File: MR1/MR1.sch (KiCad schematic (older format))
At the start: 16 parts, among them J1 Conn_01x04_Male, J2 Conn_01x04_Male, J3 Conn_01x04_Male, J4 Conn_01x04_Male, J5 Conn_01x02_Male, J6 Conn_01x04_Male, J7 Conn_01x04_Male, J8 Conn_01x04_Male, Q1 2SC1815, U5 LPC1768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

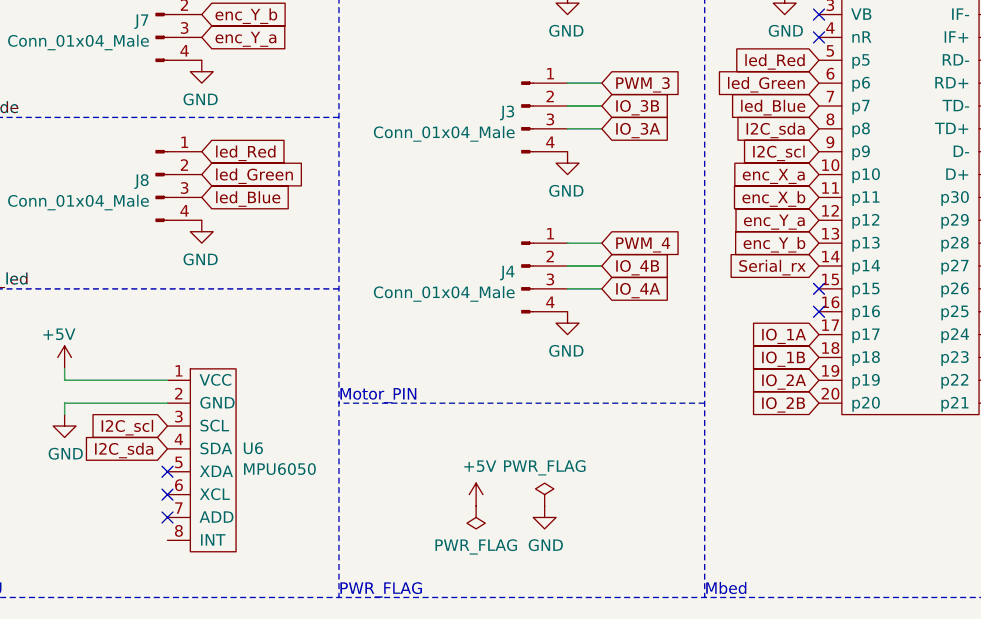
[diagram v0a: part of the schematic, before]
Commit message: update:MR1の基板完成
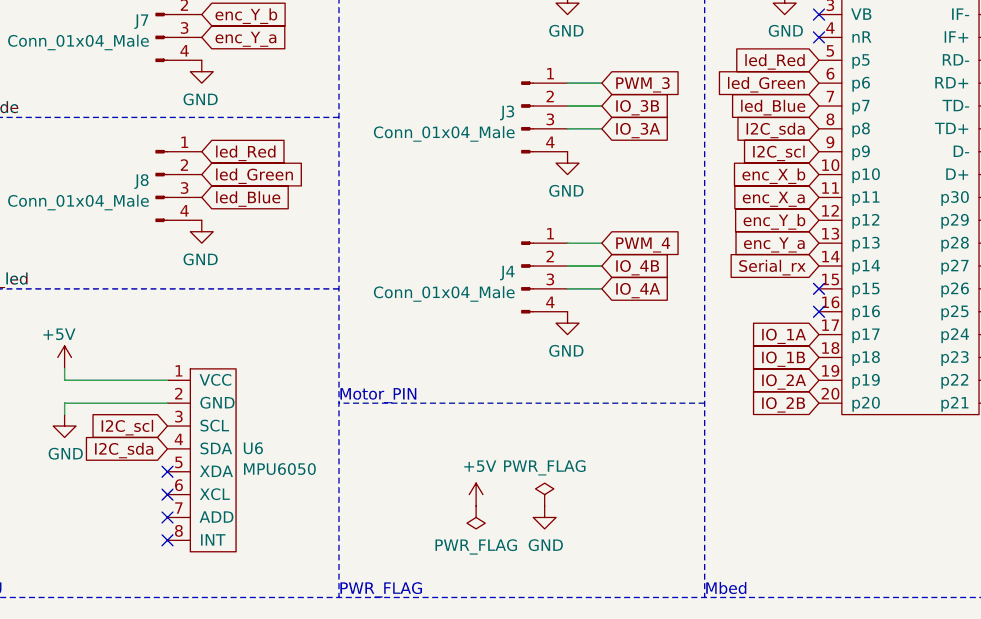
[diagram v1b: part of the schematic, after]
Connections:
- net enc_X_a: now also U5.11 (p11); no longer U5.10 (p10)
- net enc_X_b: now also U5.10 (p10); no longer U5.11 (p11)
- net enc_Y_a: now also U5.13 (p13); no longer U5.12 (p12)
- net enc_Y_b: now also U5.12 (p12); no longer U5.13 (p13)
- no-connect marks 18 -> 19
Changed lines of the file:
@@
 EESchema Schematic File Version 4
+LIBS:MR1-cache
 EELAYER 29 0
 EELAYER END
@@
 Text Notes 3200 4950 0    50   ~ 0
 Motor_PIN
-Text GLabel 5300 4150 0    50   Input ~ 0
+Text GLabel 5300 4250 0    50   Input ~ 0
 enc_Y_a
+Text GLabel 5300 4050 0    50   Input ~ 0
+enc_X_a
 Text GLabel 5300 3950 0    50   Input ~ 0
-enc_X_a
-Text GLabel 5300 4050 0    50   Input ~ 0
 enc_X_b
 Text GLabel 2600 3250 2    50   Input ~ 0
@@
 	1    0    0    -1
 $EndComp
-Text GLabel 5300 4250 0    50   Input ~ 0
+Text GLabel 5300 4150 0    50   Input ~ 0
 enc_Y_b
 Wire Notes Line
@@
 Text Label 1550 4450 0    50   ~ 0
 tape_led
+NoConn ~ 2450 5550
 $EndSCHEMATC

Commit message: fix: MR1
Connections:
- net I2C_scl: now also U5.10 (p10); no longer U5.9 (p9)
- net I2C_sda: now also U5.9 (p9); no longer U5.8 (p8)
- net enc_X_a: now also U5.12 (p12); no longer U5.11 (p11)
- net enc_X_b: now also U5.11 (p11); no longer U5.10 (p10)
- net enc_Y_a: now also U5.16 (p16); no longer U5.13 (p13)
- net enc_Y_b: now also U5.15 (p15); no longer U5.12 (p12)
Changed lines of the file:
@@
 Text GLabel 5300 4350 0    50   Input ~ 0
 Serial_rx
+Text GLabel 5300 3950 0    50   Input ~ 0
+I2C_scl
 Text GLabel 5300 3850 0    50   Input ~ 0
-I2C_scl
-Text GLabel 5300 3750 0    50   Input ~ 0
 I2C_sda
 Text GLabel 5300 4650 0    50   Input ~ 0
@@
 NoConn ~ 6100 3850
 NoConn ~ 6100 3950
-NoConn ~ 5300 4450
-NoConn ~ 5300 4550
 NoConn ~ 5300 3250
 NoConn ~ 5300 3350
@@
 Text Notes 3200 4950 0    50   ~ 0
 Motor_PIN
-Text GLabel 5300 4250 0    50   Input ~ 0
+Text GLabel 5300 4550 0    50   Input ~ 0
 enc_Y_a
-Text GLabel 5300 4050 0    50   Input ~ 0
-enc_X_a
-Text GLabel 5300 3950 0    50   Input ~ 0
-enc_X_b
 Text GLabel 2600 3250 2    50   Input ~ 0
 enc_Y_b
@@
 	1    0    0    -1
 $EndComp
-Text GLabel 5300 4150 0    50   Input ~ 0
+Text GLabel 5300 4450 0    50   Input ~ 0
 enc_Y_b
 Wire Notes Line
@@
 tape_led
 NoConn ~ 2450 5550
+NoConn ~ 5300 4250
+Text GLabel 5300 4050 0    50   Input ~ 0
+enc_X_b
+Text GLabel 5300 4150 0    50   Input ~ 0
+enc_X_a
+NoConn ~ 5300 3750
 $EndSCHEMATC

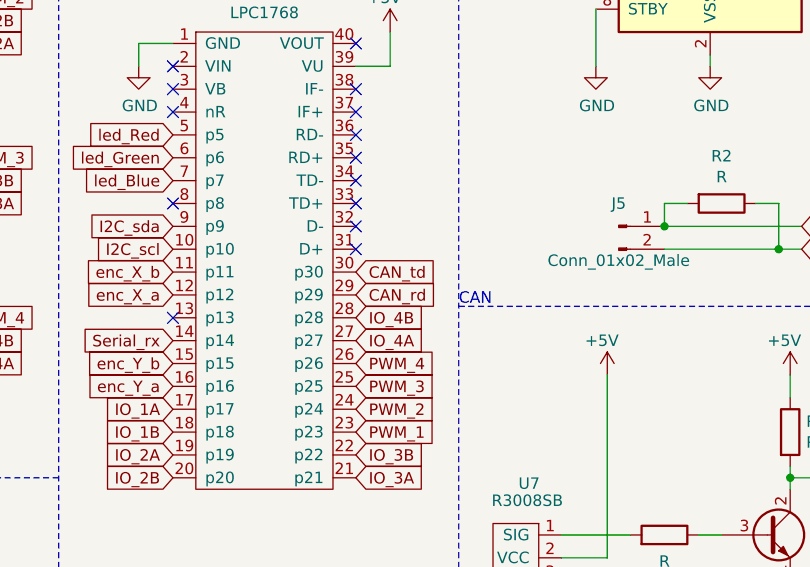
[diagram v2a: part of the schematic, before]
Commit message: update:設計変更に伴う改修、CAN通信周りの不具合を修正
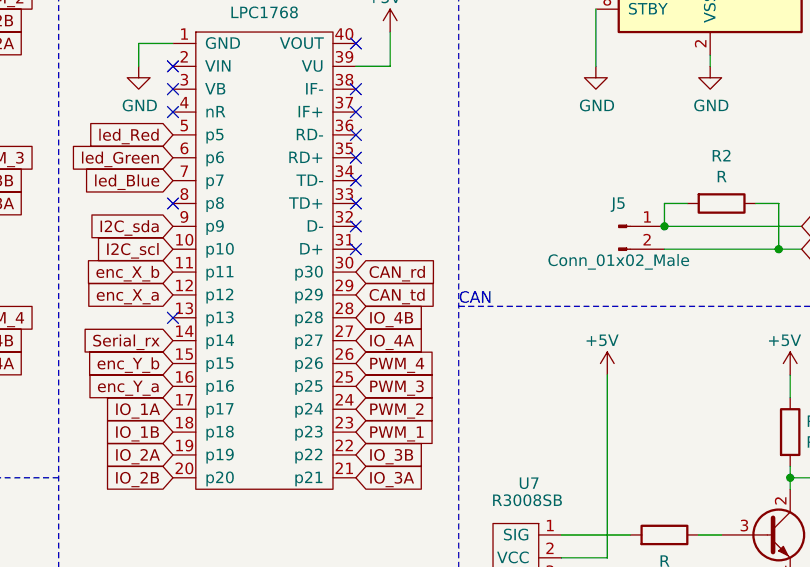
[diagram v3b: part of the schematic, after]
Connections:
- net CAN_rd: now also U5.30 (p30); no longer U5.29 (p29)
- net CAN_td: now also U5.29 (p29); no longer U5.30 (p30)
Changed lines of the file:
@@
 Text GLabel 8150 4950 2    50   Input ~ 0
 Serial_rx
+Text GLabel 6100 4150 2    50   Input ~ 0
+CAN_td
 Text GLabel 6100 4050 2    50   Input ~ 0
-CAN_td
-Text GLabel 6100 4150 2    50   Input ~ 0
 CAN_rd
 Text GLabel 6100 4250 2    50   Input ~ 0

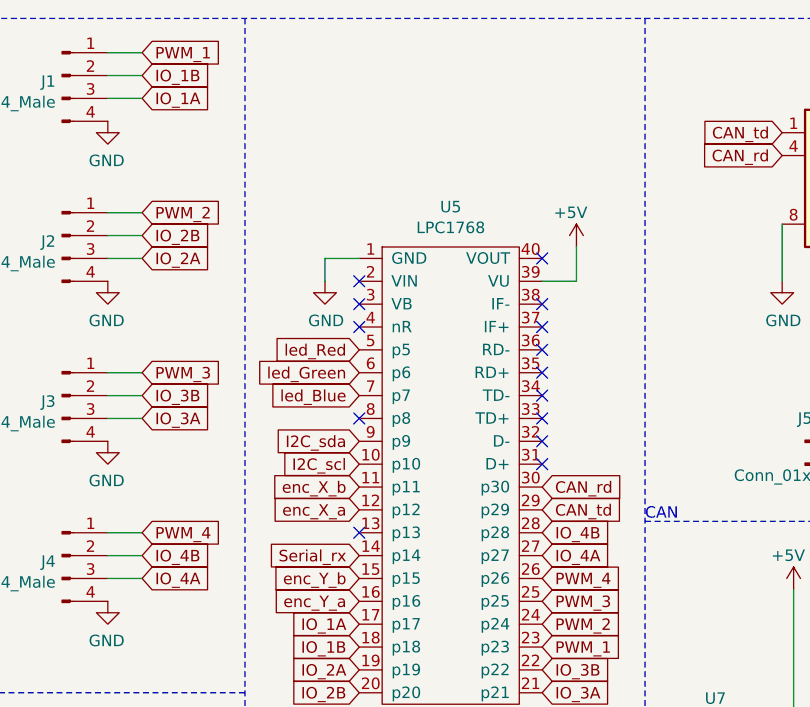
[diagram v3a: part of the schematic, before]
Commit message: update : mr1:sub_swの追加   mr2:エンコーダーの増設
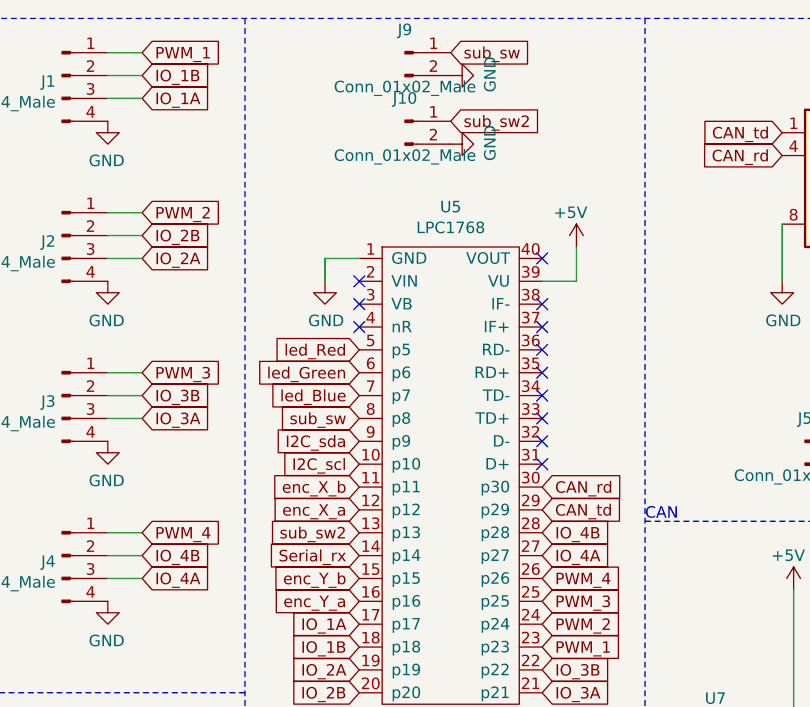
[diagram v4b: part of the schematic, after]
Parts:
- added J10, J9: Conn_01x02_Male, Connector_JST:JST_XH_B2B-XH-A_1x02_P2.50mm_Vertical, symbol Connector:Conn_01x02_Male
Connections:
- net GND: now also J10.2 (Pin_2), J9.2 (Pin_2)
- net sub_sw2: now reaches U5.13 (p13)
- net sub_sw2: now also J10.1 (Pin_1)
- net sub_sw: now reaches U5.8 (p8)
- net sub_sw: now also J9.1 (Pin_1)
- no-connect marks 19 -> 17
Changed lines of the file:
@@
 tape_led
 NoConn ~ 2450 5550
-NoConn ~ 5300 4250
 Text GLabel 5300 4050 0    50   Input ~ 0
 enc_X_b
 Text GLabel 5300 4150 0    50   Input ~ 0
 enc_X_a
-NoConn ~ 5300 3750
+Text GLabel 5300 3750 0    50   Input ~ 0
+sub_sw
+Text GLabel 5300 4250 0    50   Input ~ 0
+sub_sw2
+$Comp
+L Connector:Conn_01x02_Male J9
+U 1 1 5D7B3824
+P 5500 2150
+F 0 "J9" H 5500 2250 50  0000 C CNN
+F 1 "Conn_01x02_Male" H 5500 2000 50  0000 C CNN
+F 2 "Connector_JST:JST_XH_B2B-XH-A_1x02_P2.50mm_Vertical" H 5500 2150 50  0001 C CNN
+F 3 "~" H 5500 2150 50  0001 C CNN
+	1    5500 2150
+	1    0    0    -1
+$EndComp
+$Comp
+L Connector:Conn_01x02_Male J10
+U 1 1 5D7B5860
+P 5500 2450
+F 0 "J10" H 5500 2550 50  0000 C CNN
+F 1 "Conn_01x02_Male" H 5500 2300 50  0000 C CNN
+F 2 "Connector_JST:JST_XH_B2B-XH-A_1x02_P2.50mm_Vertical" H 5500 2450 50  0001 C CNN
+F 3 "~" H 5500 2450 50  0001 C CNN
+	1    5500 2450
+	1    0    0    -1
+$EndComp
+Text GLabel 5700 2150 2    50   Input ~ 0
+sub_sw
+Text GLabel 5700 2450 2    50   Input ~ 0
+sub_sw2
+$Comp
+L power:GND #PWR0103
+U 1 1 5D7B9A66
+P 5700 2550
+F 0 "#PWR0103" H 5700 2300 50  0001 C CNN
+F 1 "GND" H 5705 2377 50  0000 C CNN
+F 2 "" H 5700 2550 50  0001 C CNN
+F 3 "" H 5700 2550 50  0001 C CNN
+	1    5700 2550
+	0    -1   -1   0
+$EndComp
+$Comp
+L power:GND #PWR0104
+U 1 1 5D7BB29E
+P 5700 2250
+F 0 "#PWR0104" H 5700 2000 50  0001 C CNN
+F 1 "GND" H 5705 2077 50  0000 C CNN
+F 2 "" H 5700 2250 50  0001 C CNN
+F 3 "" H 5700 2250 50  0001 C CNN
+	1    5700 2250
+	0    -1   -1   0
+$EndComp
 $EndSCHEMATC
